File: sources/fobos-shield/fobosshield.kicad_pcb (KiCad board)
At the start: 2 copper layers, 83.8 x 63.5 mm, 154 parts, among them J1 Target, J10 ADCin, J11 PP1, J12 PP2, J13 Clock, J14 Trigger, J15 CSM5VCur, J16 Conn_01x01, J17 Barrel_Jack_Switch, J18 Conn_01x02, J19 Conn_01x02, J2 Glitch, J20 CSM3V3Cur, J21 GND, J22 GND, J3 Analog, J4 IOH, J5 SPI, J6 Analog2, J7 Power, J8 IOL, J9 SPI2, Q1 IRF7807Z, Q2 IRLML2502, Q3 BSS123, U1 RB-0509D, U10 INA225, U11 INA225, U12 LD1117S33TR_SOT223, U2 REE-0505S, U3 LM317L_SO8, U4 LM337L_SO8, U5 LD59015, U6 LD3985G33R_TSOT23, U7 AD8331, U8 TPS7A7100_VQFN20, U9 AD9215

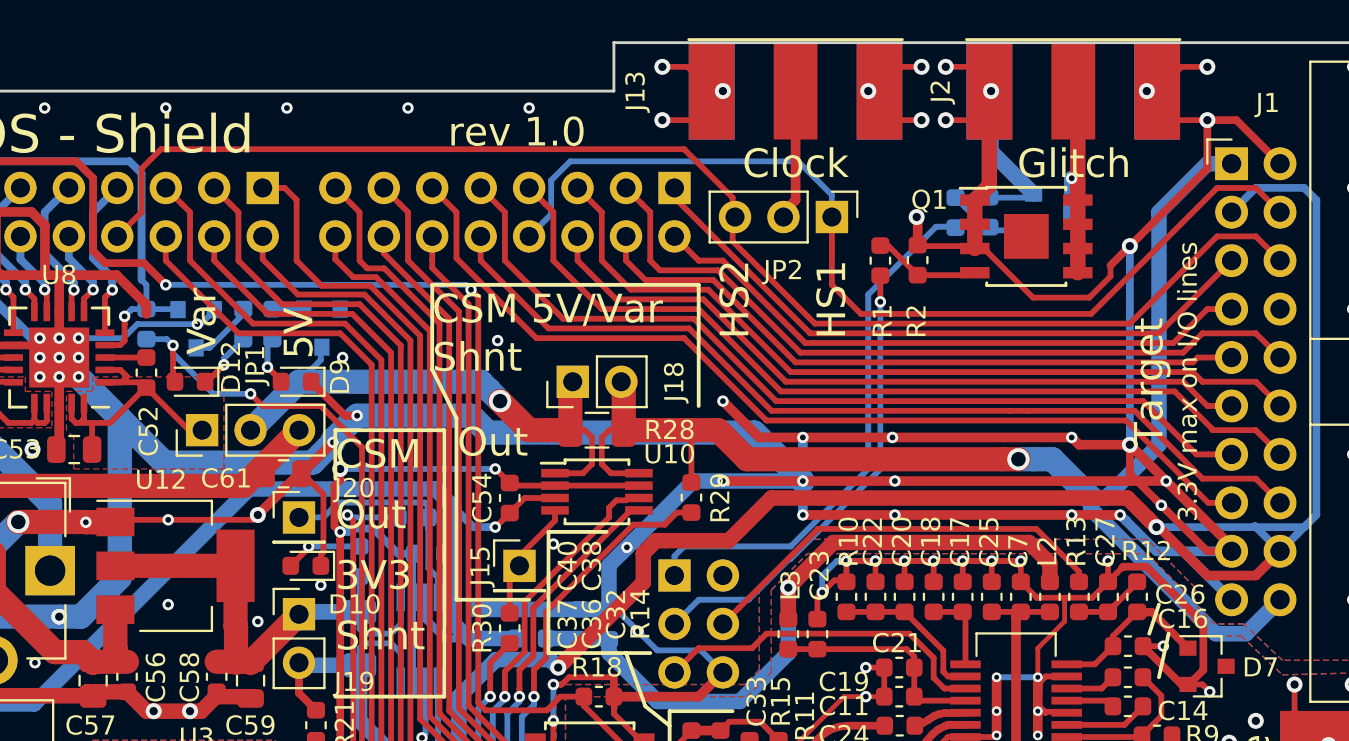
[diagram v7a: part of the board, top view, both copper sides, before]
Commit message: dut connectors and glitch verified
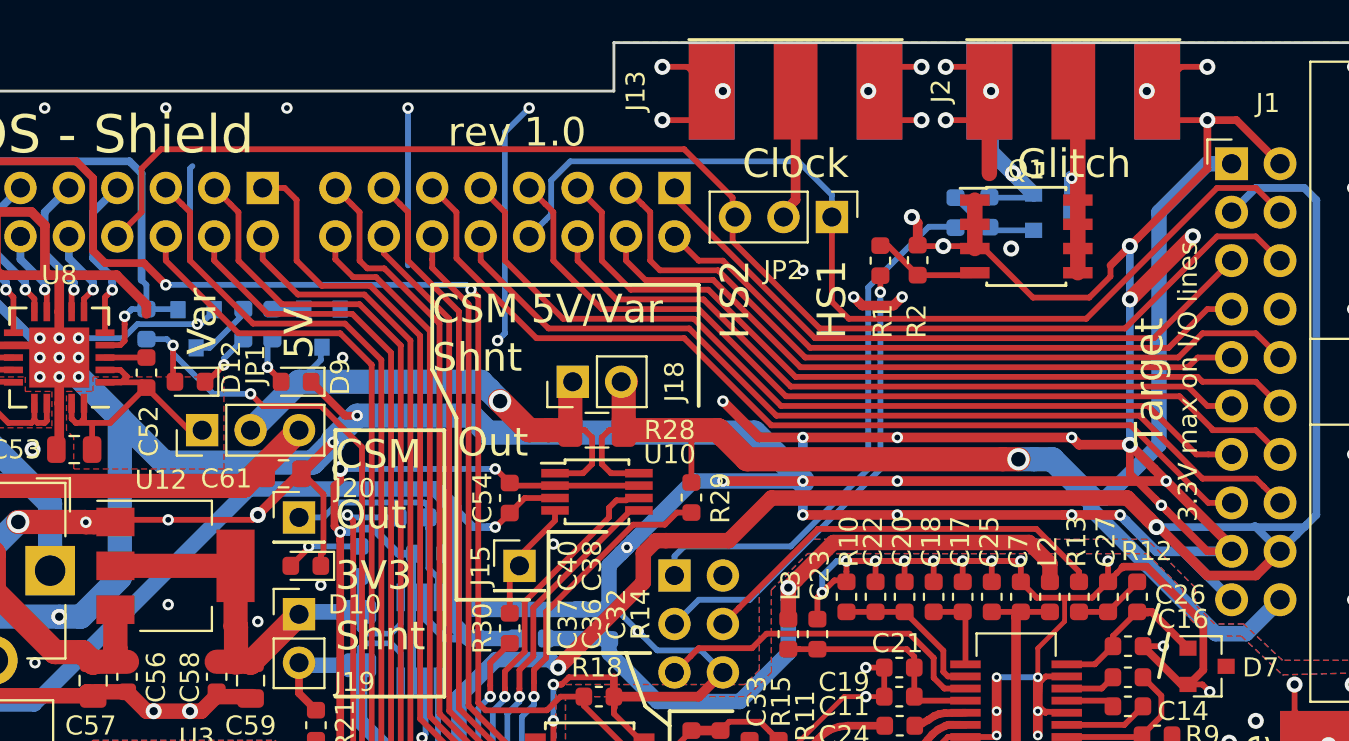
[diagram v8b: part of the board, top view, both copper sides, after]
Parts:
- D8: value 2V3 -> 2V4
- Q1: footprint Package_SO:SOIC-8-1EP_3.9x4.9mm_P1.27mm_EP2.35x2.35mm -> Package_SO:SOIC-8_3.9x4.9mm_P1.27mm
- Q3: value BSS123 -> BSS138L
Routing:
- net GND: track 472.3 -> 499.5 mm, vias 106 -> 114
- net (no net): track 0.00 -> 5.01 mm
- net CW_HS1: track 51.6 -> 52.4 mm
